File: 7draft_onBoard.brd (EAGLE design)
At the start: 89.8 x 88.9 mm, 73 parts, among them IC3 74ABT125PW, IC4 MAX4466KS, J2 USB_MINI-B_DIGIKEY, Q1 NPN 40V 1A SOT-23

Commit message: added led's so we know when board has power and is able to blink
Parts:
- added LED1, LED4, LED5: (no value), SparkFun-LED:LED-0603
- added R25, R26, R27: 1k, SparkFun-Retired:0603
- moved OSC 72.8 mm to (44.6, 39.5), turned to 225 degrees
- moved MPU6050 27.4 mm to (15.2, 78.7)
- turned ATMEGA328P-AU to 315 degrees
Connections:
- new net N$3: LED1.A, R25.1
- new net N$4: LED4.A, R26.1
- new net N$5: LED5.A, R27.1
- net 5V: now also R26.2, R27.2
- net D9: now also R25.2
- net GND: now also LED1.C
- net RXLED: now also LED4.C
- net TXLED: now also LED5.C
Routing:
- net A6: track 0.00 -> 25.5 mm
- net A7: track 0.00 -> 22.4 mm
- net D2: track 0.00 -> 15.5 mm, vias 0 -> 1
- net MISO: track 0.00 -> 11.0 mm
- net D3: track 0.00 -> 10.2 mm
- net GND: track 23.1 -> 33.1 mm, vias 0 -> 2
- net SCK: track 0.00 -> 9.68 mm
- net D4: track 0.00 -> 8.91 mm
- net MOSI: track 0.00 -> 8.83 mm
- net SCL: track 0.00 -> 8.75 mm
- net D5: track 0.00 -> 8.25 mm
- net D6: track 0.00 -> 8.16 mm
- net SS: track 0.00 -> 7.44 mm
- net D7: track 0.00 -> 7.29 mm
- net D8: track 0.00 -> 6.40 mm
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
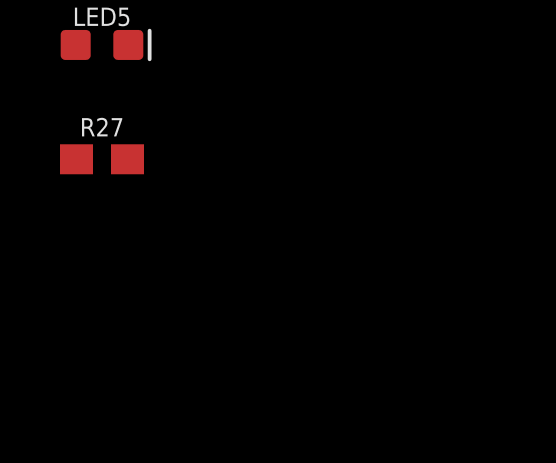
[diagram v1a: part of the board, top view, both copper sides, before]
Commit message: added leds for RX, TX, power
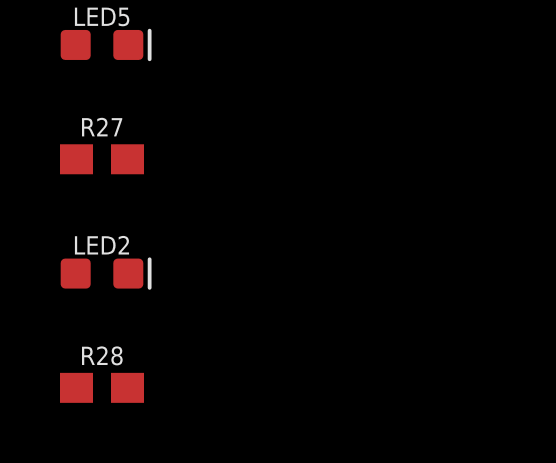
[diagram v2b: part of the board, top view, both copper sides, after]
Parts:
- added LED2: (no value), SparkFun-LED:LED-0603
- added R28: 1k, SparkFun-Retired:0603
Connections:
- new net N$7: LED2.A, R28.1
- net 5V: now also R28.2
- net GND: now also LED2.C
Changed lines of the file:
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@@
 <attribute name="PROD_ID" value="RES-09288" x="-86.36" y="-44.45" size="1.778" layer="27" display="off"/>
+</element>
+<element name="LED2" library="SparkFun-LED" package="LED-0603" value="" x="-86.36" y="-48.26"/>
+<element name="R28" library="SparkFun-Retired" package="0603" value="1k" x="-86.36" y="-52.07">
+<attribute name="PROD_ID" value="RES-09288" x="-86.36" y="-52.07" size="1.778" layer="27" display="off"/>
 </element>
 </elements>
@@
 <wire x1="46.99" y1="36.001259375" x2="45.862225" y2="37.129034375" width="0.2032" layer="1"/>
 <contactref element="LED1" pad="C"/>
+<contactref element="LED2" pad="C"/>
 <wire x1="64.2112" y1="76.2" x2="70.409" y2="76.2" width="0" layer="19" extent="1-1"/>
 <wire x1="56.258" y1="83.185" x2="59.69" y2="76.0222" width="0" layer="19" extent="1-1"/>
@@
 <wire x1="83.82" y1="38.1" x2="52.435771875" y2="31.7049625" width="0" layer="19" extent="1-1"/>
 <wire x1="-85.483" y1="-17.78" x2="-36.83" y2="6.35" width="0" layer="19" extent="1-1"/>
+<wire x1="-85.483" y1="-48.26" x2="-85.483" y2="-17.78" width="0" layer="19" extent="1-1"/>
 </signal>
 <signal name="N$6">
@@
 <contactref element="R27" pad="2"/>
 <contactref element="R26" pad="2"/>
-<wire x1="57.15" y1="50.8" x2="64.77" y2="68.58" width="0" layer="19" extent="1-1"/>
-<wire x1="46.4369625" y1="37.703771875" x2="57.15" y2="50.8" width="0" layer="19" extent="1-1"/>
-<wire x1="45.30545" y1="36.572259375" x2="46.4369625" y2="37.703771875" width="0" layer="19" extent="1-1"/>
+<contactref element="R28" pad="2"/>
+<wire x1="-85.51" y1="-44.45" x2="-85.51" y2="-52.07" width="0" layer="19" extent="1-1"/>
+<wire x1="-85.51" y1="-36.83" x2="-85.51" y2="-44.45" width="0" layer="19" extent="1-1"/>
+<wire x1="-30.08" y1="8.95" x2="-85.51" y2="-36.83" width="0" layer="19" extent="1-1"/>
+<wire x1="-19.73" y1="32.135" x2="-30.08" y2="8.95" width="0" layer="19" extent="1-1"/>
+<wire x1="-19.08" y1="32.135" x2="-19.73" y2="32.135" width="0" layer="19" extent="1-1"/>
+<wire x1="-18.43" y1="32.135" x2="-19.08" y2="32.135" width="0" layer="19" extent="1-1"/>
+<wire x1="-17.78" y1="32.135" x2="-18.43" y2="32.135" width="0" layer="19" extent="1-1"/>
+<wire x1="8.89" y1="30.48" x2="-17.78" y2="32.135" width="0" layer="19" extent="1-1"/>
+<wire x1="21.59" y1="32.805" x2="8.89" y2="30.48" width="0" layer="19" extent="1-1"/>
+<wire x1="23.48" y1="32.55" x2="21.59" y2="32.805" width="0" layer="19" extent="1-1"/>
+<wire x1="45.30545" y1="36.572259375" x2="23.48" y2="32.55" width="0" layer="19" extent="1-1"/>
+<wire x1="46.4369625" y1="37.703771875" x2="45.30545" y2="36.572259375" width="0" layer="19" extent="1-1"/>
 <wire x1="50.729525" y1="29.9987125" x2="45.30545" y2="36.572259375" width="0" layer="19" extent="1-1"/>
-<wire x1="23.48" y1="32.55" x2="45.30545" y2="36.572259375" width="0" layer="19" extent="1-1"/>
-<wire x1="21.59" y1="32.805" x2="23.48" y2="32.55" width="0" layer="19" extent="1-1"/>
-<wire x1="8.89" y1="30.48" x2="21.59" y2="32.805" width="0" layer="19" extent="1-1"/>
+<wire x1="57.15" y1="50.8" x2="46.4369625" y2="37.703771875" width="0" layer="19" extent="1-1"/>
+<wire x1="64.77" y1="68.58" x2="57.15" y2="50.8" width="0" layer="19" extent="1-1"/>
 <wire x1="44.45" y1="83.82" x2="64.77" y2="68.58" width="0" layer="19" extent="1-1"/>
 <wire x1="30.48" y1="67.31" x2="44.45" y2="83.82" width="0" layer="19" extent="1-1"/>
 <wire x1="17.14" y1="77.49" x2="30.48" y2="67.31" width="0" layer="19" extent="1-1"/>
-<wire x1="-17.78" y1="32.135" x2="8.89" y2="30.48" width="0" layer="19" extent="1-1"/>
-<wire x1="-18.43" y1="32.135" x2="-17.78" y2="32.135" width="0" layer="19" extent="1-1"/>
-<wire x1="-19.08" y1="32.135" x2="-18.43" y2="32.135" width="0" layer="19" extent="1-1"/>
-<wire x1="-19.73" y1="32.135" x2="-19.08" y2="32.135" width="0" layer="19" extent="1-1"/>
-<wire x1="-30.08" y1="8.95" x2="-19.73" y2="32.135" width="0" layer="19" extent="1-1"/>
 <wire x1="83.82" y1="35.56" x2="57.15" y2="50.8" width="0" layer="19" extent="1-1"/>
 <wire x1="-19.9" y1="74.93" x2="17.14" y2="77.49" width="0" layer="19" extent="1-1"/>
@@
 <wire x1="-72.5678" y1="66.04" x2="-66.04" y2="62.23" width="0" layer="19" extent="1-1"/>
 <wire x1="-66.89" y1="71.12" x2="-72.5678" y2="66.04" width="0" layer="19" extent="1-1"/>
-<wire x1="-85.51" y1="-36.83" x2="-30.08" y2="8.95" width="0" layer="19" extent="1-1"/>
-<wire x1="-85.51" y1="-44.45" x2="-85.51" y2="-36.83" width="0" layer="19" extent="1-1"/>
 </signal>
 <signal name="RESET">
@@
 <wire x1="-87.237" y1="-40.64" x2="-87.21" y2="-44.45" width="0" layer="19" extent="1-1"/>
 </signal>
+<signal name="N$7">
+<contactref element="LED2" pad="A"/>
+<contactref element="R28" pad="1"/>
+<wire x1="-87.237" y1="-48.26" x2="-87.21" y2="-52.07" width="0" layer="19" extent="1-1"/>
+</signal>
 </signals>

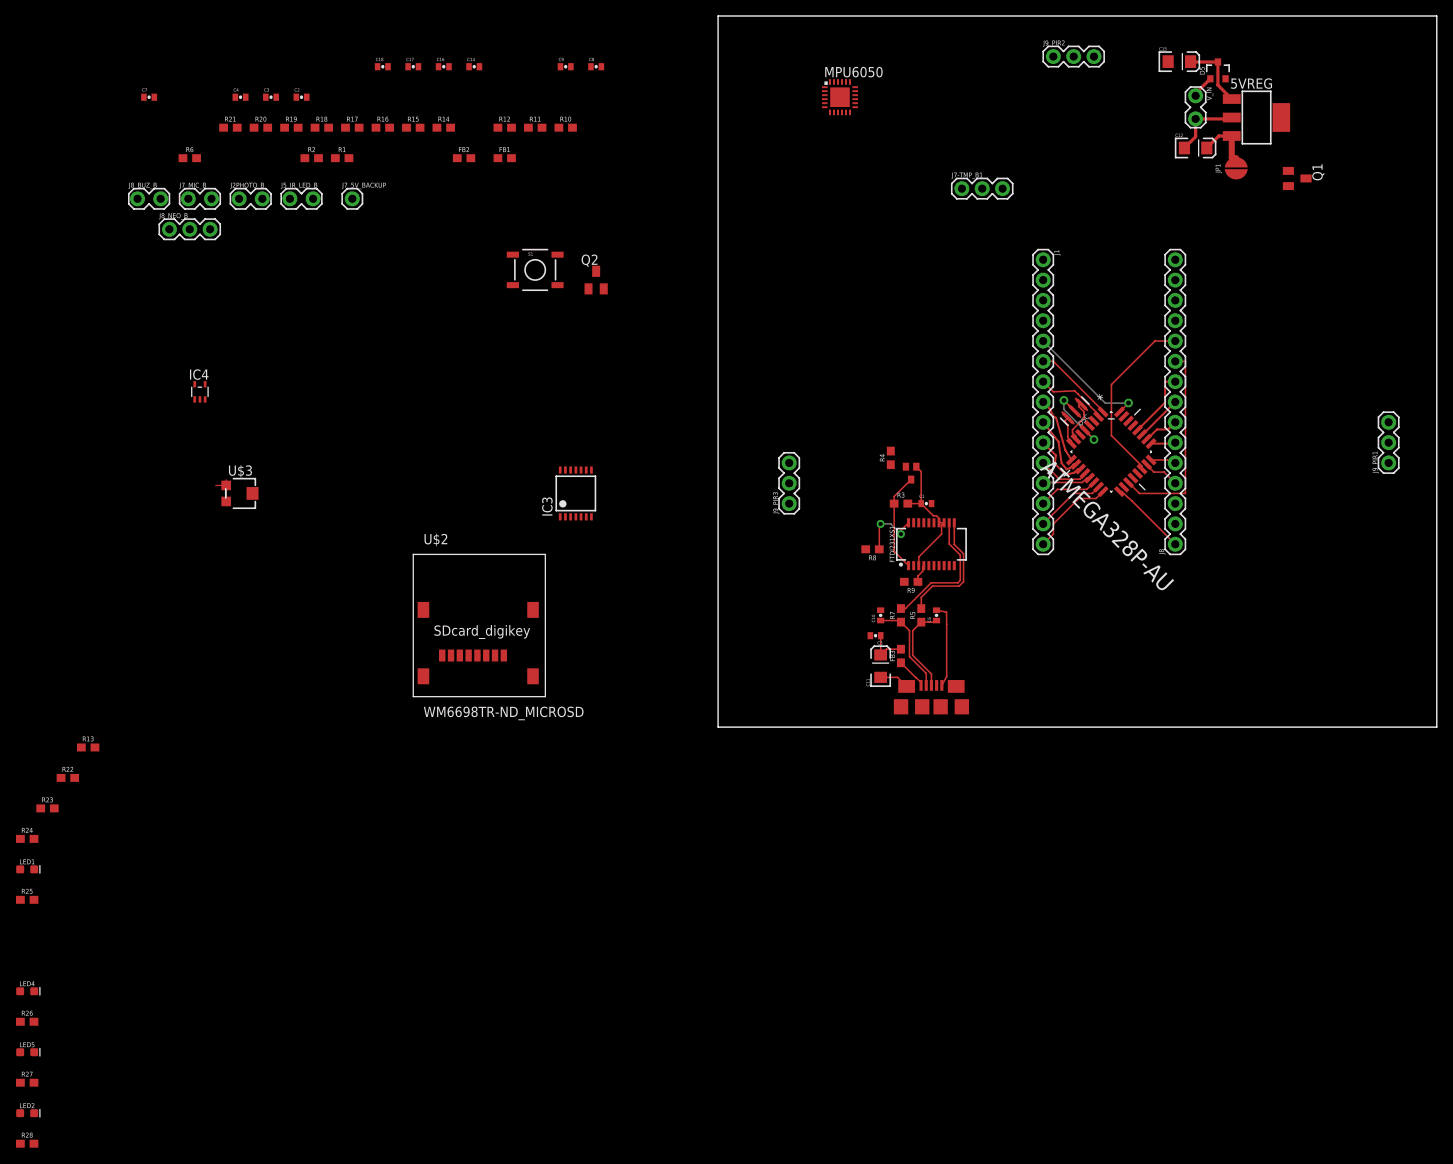
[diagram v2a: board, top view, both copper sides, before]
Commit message: less condensed version, indicator leds. and more resistors for IR led
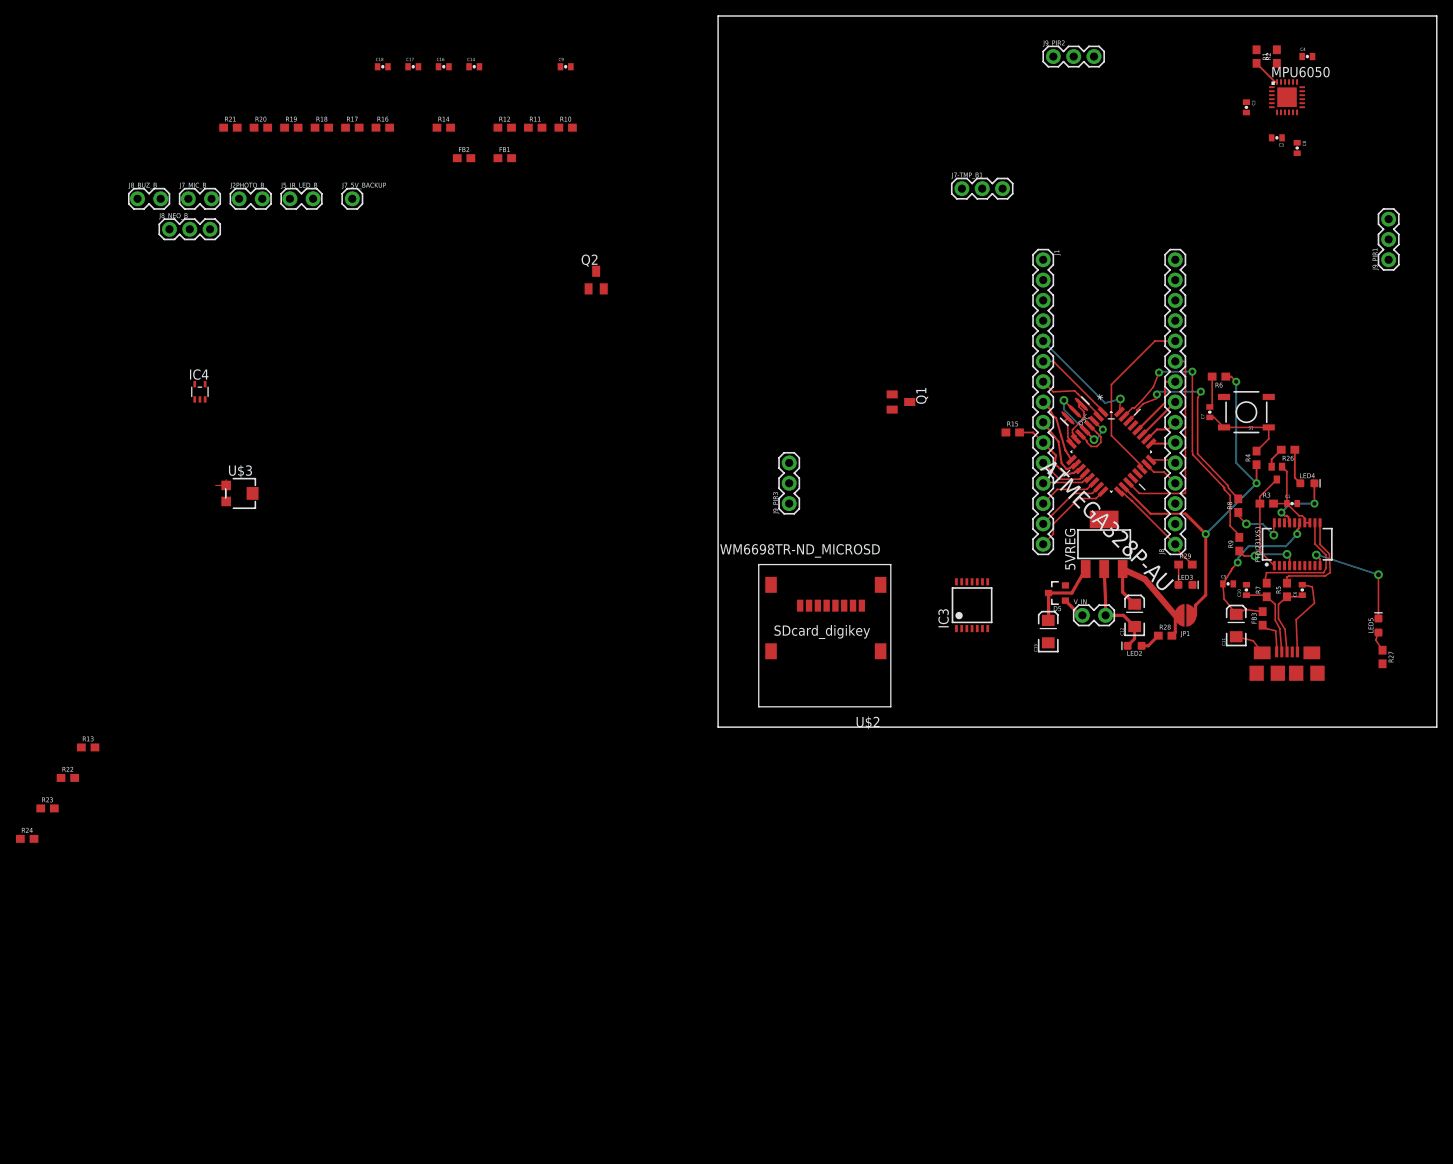
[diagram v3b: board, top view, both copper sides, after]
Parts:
- removed LED1: (no value), SparkFun-LED:LED-0603
- removed R25: 1k, SparkFun-Retired:0603
- added LED3: (no value), SparkFun-LED:LED-0603
- added R29: 1k, SparkFun-Retired:0603
- moved R27 177.6 mm to (83.1, 8.76), turned to 270 degrees
- moved LED5 177.1 mm to (82.5, 12.7), turned to 90 degrees
- moved R26 173.1 mm to (71.2, 34.7), turned to 180 degrees
- moved LED4 172.2 mm to (73.7, 30.5)
- moved R28 155.8 mm to (55.9, 11.4)
- moved LED2 150.3 mm to (52.1, 10.2), turned to 180 degrees
- moved C7 138.3 mm to (61.5, 39.4), turned to 90 degrees
- moved C4 133.4 mm to (73.7, 83.8)
- moved R6 131.5 mm to (62.6, 43.8), turned to 180 degrees
- moved C3 125.8 mm to (69.8, 73.7), turned to 180 degrees
- moved R2 121.3 mm to (69.8, 83.8), turned to 90 degrees
- moved C2 118.1 mm to (66.0, 77.5), turned to 270 degrees
- moved R1 115.0 mm to (67.3, 83.8), turned to 270 degrees
- moved S1 90.7 mm to (66.0, 39.4), turned to 180 degrees
- moved C8 88.2 mm to (72.4, 72.4), turned to 270 degrees
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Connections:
- net N$4 renamed LED4
- net N$5 renamed LED5
- net N$7 renamed POWERLED
- net RX-I renamed TX-O_N
- net TX-O renamed TX-O_P
- removed net N$3: LED1.A, R25.1
- new net N$4: LED3.A, R29.1
- net 5REGOUT: now also R28.2
- net 5V: no longer R28.2
- net D9: no longer R25.2
- net GND: now also LED3.C; no longer LED1.C
- net SCK: now also R29.2
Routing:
- net 5V: track 0.00 -> 58.8 mm, vias 0 -> 3
- net TX-O_P: track 0.00 -> 34.9 mm, vias 0 -> 2
- net TX-O_N: track 0.00 -> 26.4 mm, vias 0 -> 2
- net VUSB: track 9.15 -> 26.3 mm, vias 0 -> 2
- net TXLED: track 0.00 -> 15.2 mm, vias 0 -> 2
- net DTR: track 0.00 -> 11.5 mm
- net 5REGOUT: track 7.07 -> 16.7 mm
- net RXLED: track 0.00 -> 9.03 mm, vias 0 -> 2
- net GND: track 33.1 -> 40.7 mm, vias 2 -> 3
- net 3.3VFTDI: track 17.4 -> 10.7 mm
- net RX: track 2.32 -> 7.85 mm, vias 0 -> 2
- net LED4: track 0.00 -> 4.48 mm
- net RESET: track 0.00 -> 3.92 mm
- net SDA: track 5.84 -> 9.37 mm
- net D7: track 7.29 -> 10.8 mm
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
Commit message: Almost done, wanted to save before I change the IR leds to an equivalent resistance or a resistor array.
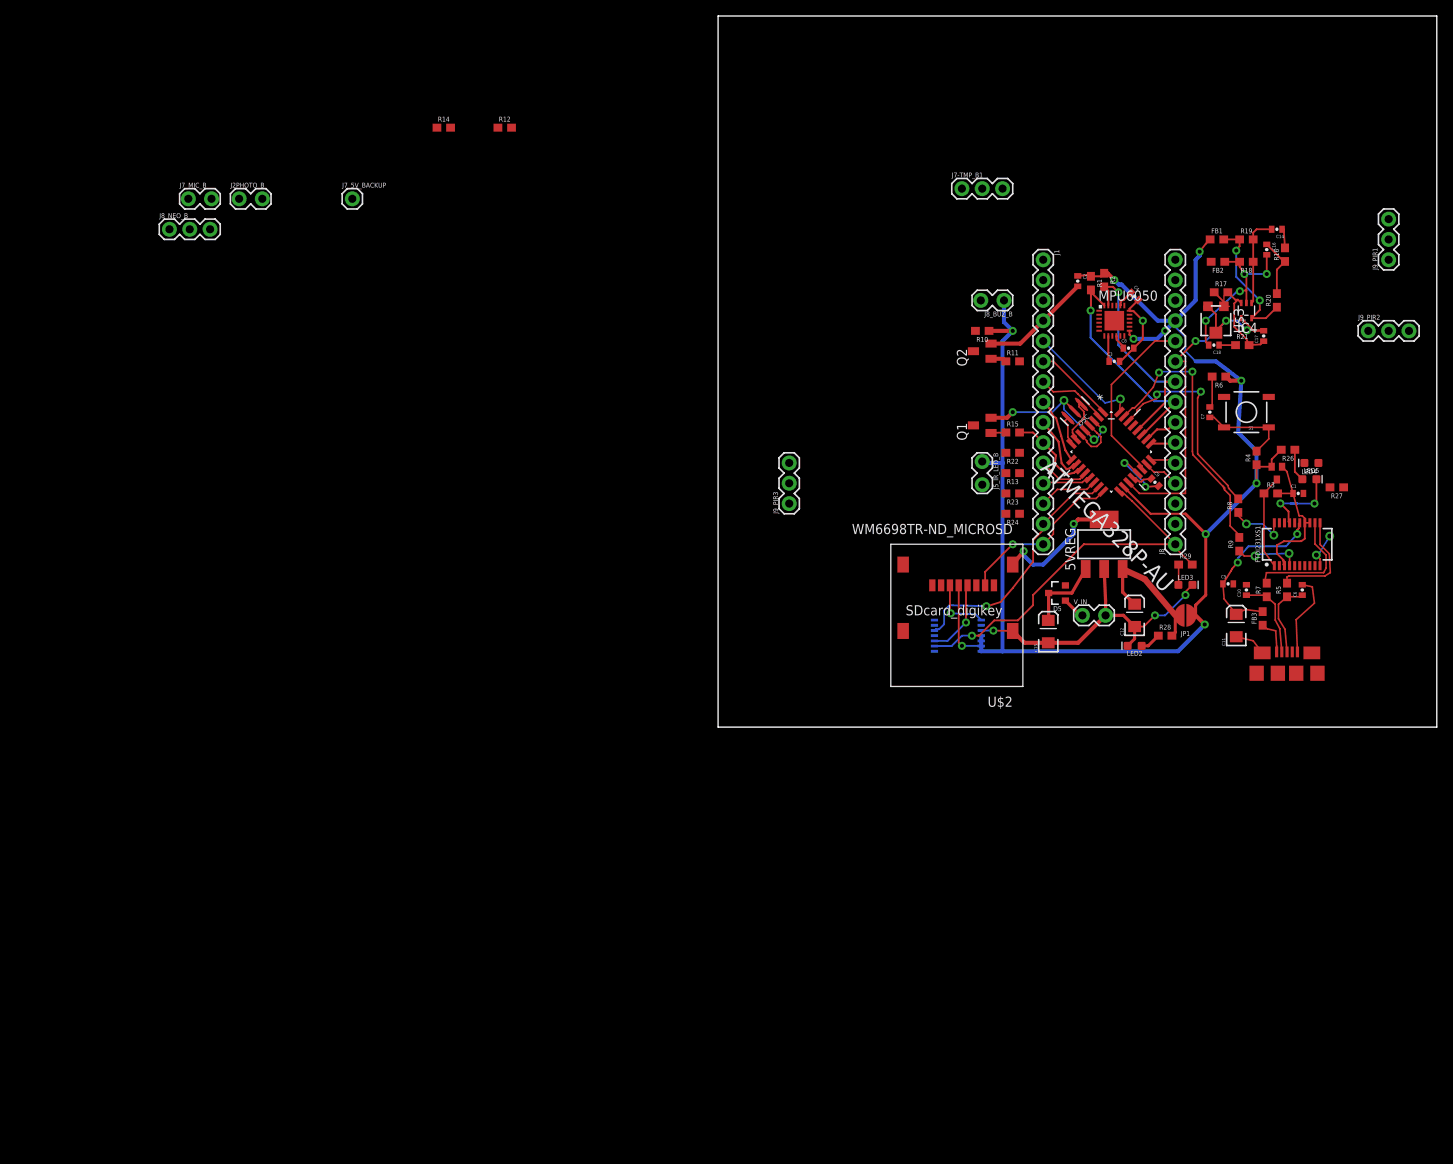
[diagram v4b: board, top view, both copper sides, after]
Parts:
- moved IC4 131.2 mm to (66.0, 52.1), turned to 180 degrees
- moved R24 129.7 mm to (36.8, 26.7), turned to 180 degrees
- moved R21 129.4 mm to (65.5, 47.8)
- moved R20 128.8 mm to (69.8, 53.3), turned to 90 degrees
- moved R23 126.9 mm to (36.8, 29.2), turned to 180 degrees
- moved R22 124.9 mm to (36.8, 34.3), turned to 180 degrees
- moved U$3 123.8 mm to (62.2, 50.8), turned to 270 degrees
- moved R13 120.5 mm to (36.8, 31.8), turned to 180 degrees
- moved R19 120.2 mm to (66.0, 61.0)
- moved R18 116.8 mm to (66.0, 58.2), turned to 180 degrees
- moved R16 113.9 mm to (70.9, 59.1), turned to 90 degrees
- moved C17 111.5 mm to (68.2, 48.9), turned to 90 degrees
- moved R17 110.5 mm to (62.9, 54.4)
- moved C18 109.6 mm to (62.0, 47.8), turned to 180 degrees
- moved J8_BUZ_B 108.7 mm to (35.6, 53.3), turned to 180 degrees
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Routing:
- net 5V: track 58.8 -> 201.7 mm, vias 3 -> 10
- net GND: track 40.7 -> 148.6 mm, vias 3 -> 16
- net SCK: track 12.8 -> 48.9 mm, vias 0 -> 1
- net A6: track 25.5 -> 47.9 mm, vias 0 -> 3
- net MOSI: track 8.83 -> 31.2 mm, vias 0 -> 1
- net SCL: track 8.75 -> 29.0 mm, vias 0 -> 1
- net SDA: track 9.37 -> 28.4 mm, vias 0 -> 1
- net AVCC: track 0.00 -> 17.3 mm, vias 0 -> 2
- net MIC_IN+: track 0.00 -> 11.4 mm
- net N$30: track 0.00 -> 10.8 mm
- net TXLED: track 15.2 -> 4.53 mm
- net MISO: track 11.0 -> 21.3 mm, vias 0 -> 1
- net SCK_BUFF: track 0.00 -> 9.61 mm, vias 0 -> 1
- net 3.3VFTDI: track 10.7 -> 19.9 mm
- net SS_BUFF: track 0.00 -> 7.64 mm, vias 0 -> 1
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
